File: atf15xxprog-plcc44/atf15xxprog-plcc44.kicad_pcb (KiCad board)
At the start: 2 copper layers, 99.1 x 27.9 mm, 8 parts, among them J1 AVR-JTAG-10, J2 Conn_01x19_Male, J3 Conn_01x19_Male, U1 atf15xx_PLCC44

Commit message: atf15xxprog-plcc44: use a custom JTAG-A symbol
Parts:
- J1: value AVR-JTAG-10 -> ATMEL JTAG-A
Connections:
- J1 pad 6: Net-(J1-Pad6) -> unconnected-(J1-Pad6)
- J1 pad 7: Net-(J1-Pad7) -> unconnected-(J1-Pad7)
- J1 pad 8: Net-(J1-Pad8) -> unconnected-(J1-Pad8)

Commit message: atf15xxprog-plcc44: fix tiny fonts in texts
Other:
- board size 99.1 x 27.9 mm -> 99.1 x 55.9 mm
- board text added: "ATF1502/ATF1504 Breakboard Adapter/Programmer Copyright (C) 2021-2022 Alvaro Polo"
- board text added: "IN/GCLR IN/OE2/GCLK2 A1 A2 A3/PD1 A4/TDI A5 A6 A7 A8 A9/TMS A10 A11 A12 A13 A14 A15 A16 B32 B31 B30 B29 B28 B27 B26 B25/TCK B24 B23 B22 B21 B20/TDO B19 B18 B17 IN/GCLK1 IN/OE1"
- board text added: "IN/GCLR IN/OE2/GCLK2 A16 A14 A11 A8/TDI A5 A4 A3/PD1 A1 B32/TMS B30 B25 B24 B21 B20 B19 B17 C33 C35/PD2 C36 C37 C40 C41 C46 C48/TCK D49 D51 D52 D53 D56/TDO D57 D62 D64/GCLK3 IN/GCLK1 IN/OE1"
- board text removed: "A1 A2 A3/PD1 A4/TDI A5 A6 A7 A8 A9/TMS A10 A11 A12 A13 A14 A15 A16 B32 B31 B30 B29 B28 B27 B26 B25/TCK B24 B23 B22 B21 B20/TDO B19 B18 B17"
- board text removed: "A16 A14 A11 A8/TDI A5 A4 A3/PD1 A1 B32/TMS B30 B25 B24 B21 B20 B19 B17 C33 C35/PD2 C36 C37 C40 C41 C46 C48/TCK D49 D51 D52 D53 D56/TDO D57 D62 D64/GCLK3"
- board text removed: "ATF1502/ATF1504 Breakboard Adapter/Programmer Copyright (C) 2021 Alvaro Polo"
- board text removed: "IN/GCLR IN/OE2/GCLK2 IN/GCLK1 IN/OE1"

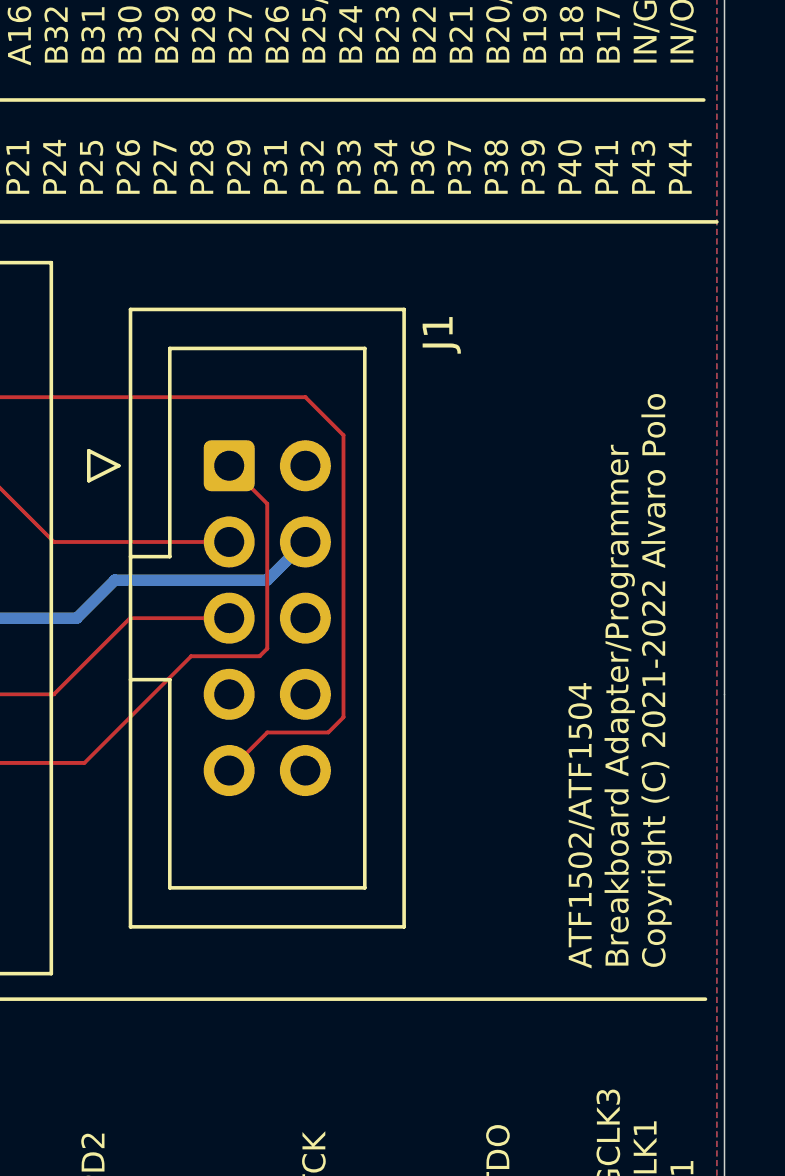
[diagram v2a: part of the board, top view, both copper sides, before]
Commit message: atf15xxprog-plcc44: add pull-up resistors for JTAG
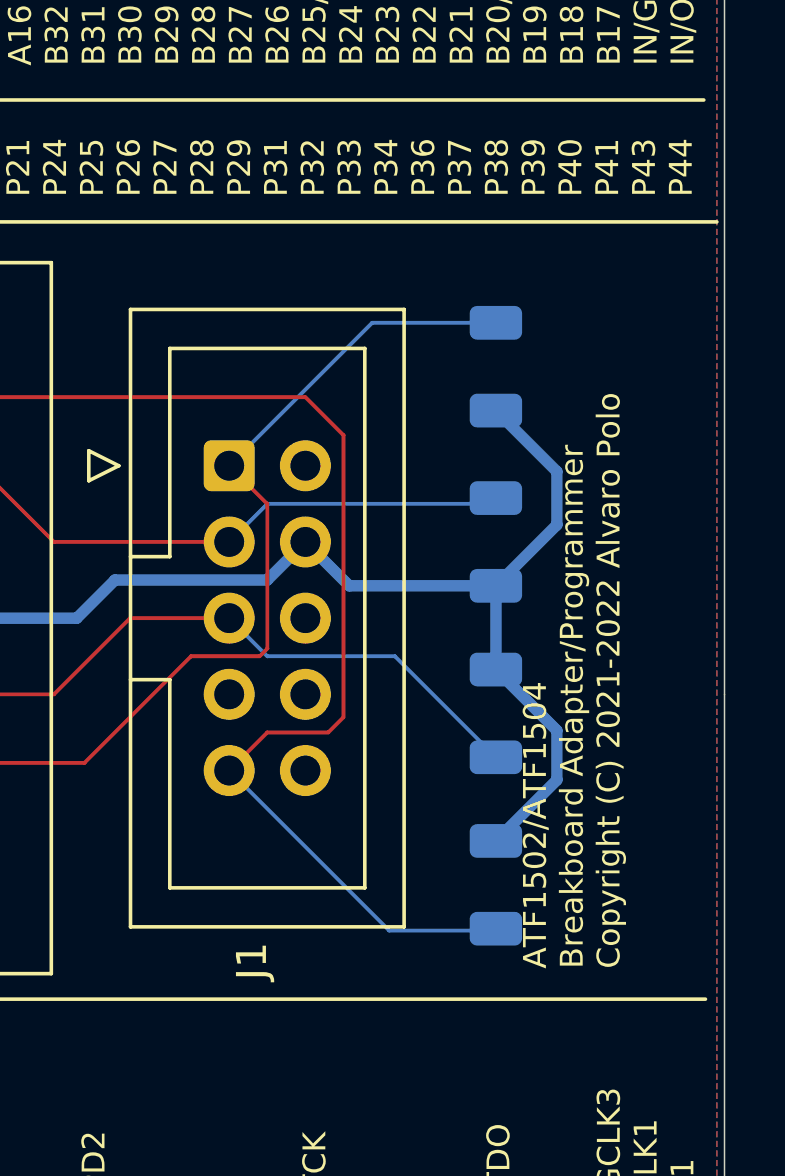
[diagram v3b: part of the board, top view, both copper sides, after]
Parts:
- added R1: 4K7, Resistor_SMD:R_1206_3216Metric, B.Cu at (165.1, 66.5)
- added R2: 4K7, Resistor_SMD:R_1206_3216Metric, B.Cu at (165.1, 78.1)
- added R3: 4K7, Resistor_SMD:R_1206_3216Metric, B.Cu at (165.1, 72.4)
- added R4: 4K7, Resistor_SMD:R_1206_3216Metric, B.Cu at (165.1, 83.8)
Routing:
- net VCC: track 120.9 -> 145.5 mm
- net /TDI-P7: track 77.7 -> 88.8 mm
- net /TCK-P32: track 77.9 -> 88.8 mm
- net /TMS-P13: track 81.0 -> 91.8 mm
- net /TDO-P38: track 71.7 -> 81.2 mm
